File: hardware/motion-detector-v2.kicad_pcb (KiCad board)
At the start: 2 copper layers, 45 x 25 mm, 33 parts, among them J1 Debug, P1 CON-SENSOR2, P2 Boot, U1 XMC110024, U3 AM612, U4 DRILL, U5 DRILL, U6 DRILL, U7 DRILL

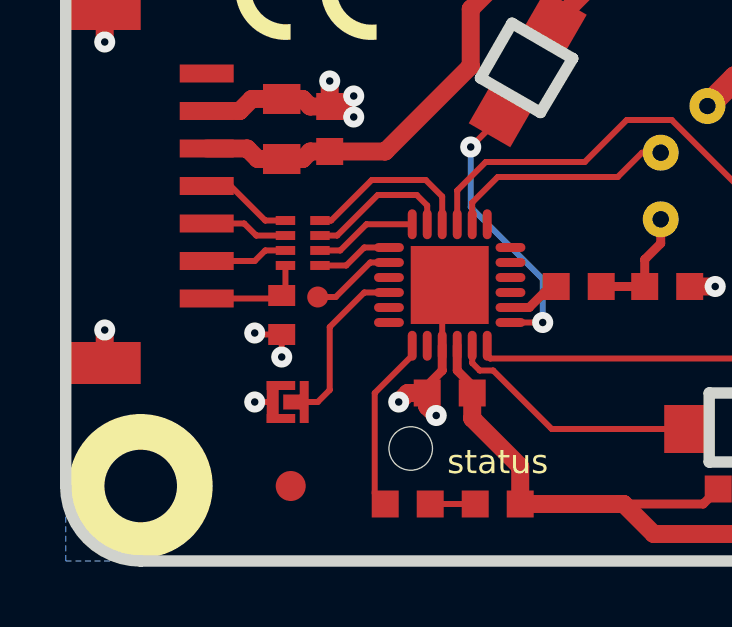
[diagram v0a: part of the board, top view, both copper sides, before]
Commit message: Change capacitor footprint(s) to C0402F
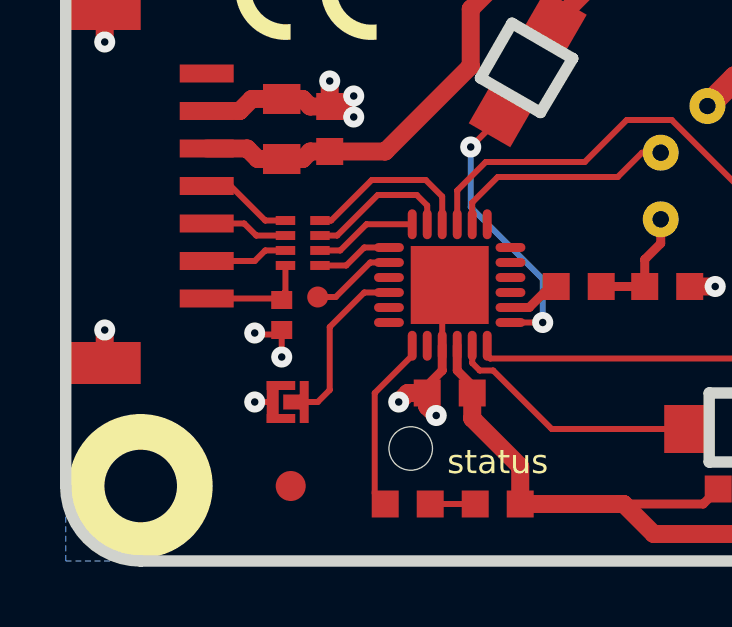
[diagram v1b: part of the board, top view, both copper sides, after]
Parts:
- C1: footprint C0402E -> kicad-libraries:C0402F
- C2: footprint C0805 -> kicad-libraries:C0805
- C3, C4, C6, C7: footprint C0603F -> kicad-libraries:C0603F
- D1: footprint D0603F -> kicad-libraries:D0603F
- R1, R2, R3, R4, R5: footprint R0603F -> kicad-libraries:R0603F
- U3: footprint AM612 -> kicad-libraries:AM612
- U4, U5, U6, U7: footprint DRILL_NP -> kicad-libraries:DRILL_NP
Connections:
- P1 pad 1: (no net) -> Net-(P1-Pad1)
- U1 pad 15: (no net) -> Net-(U1-Pad15)
- U1 pad 16: (no net) -> Net-(U1-Pad16)
- U1 pad 17: (no net) -> Net-(U1-Pad17)
- U1 pad 18: (no net) -> Net-(U1-Pad18)
- U1 pad 19: (no net) -> Net-(U1-Pad19)
- U1 pad 3: (no net) -> Net-(U1-Pad3)
- U1 pad 5: (no net) -> Net-(U1-Pad5)
- U1 pad 6: (no net) -> Net-(U1-Pad6)
- U1 pad 8: (no net) -> Net-(U1-Pad8)
